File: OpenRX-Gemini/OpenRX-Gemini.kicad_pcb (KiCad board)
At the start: 6 copper layers, 17 x 15.7 mm, 86 parts, among them J1 Conn_Coaxial_Small, J2 Conn_Coaxial_Small, T1 0900PC16J0042001E, T2 0900PC16J0042001E, U1 ESP32-C3, U2 TLV75533PDQNR, U3 LR1121IMLTRT, U4 RFX2401C, U5 SKY13373-460LF, U6 LR1121IMLTRT, U7 RFX2401C, U8 SKY13373-460LF, U9 TS2306A 240GF MSM 9_C2976675, X1 CJ17-400001010B20

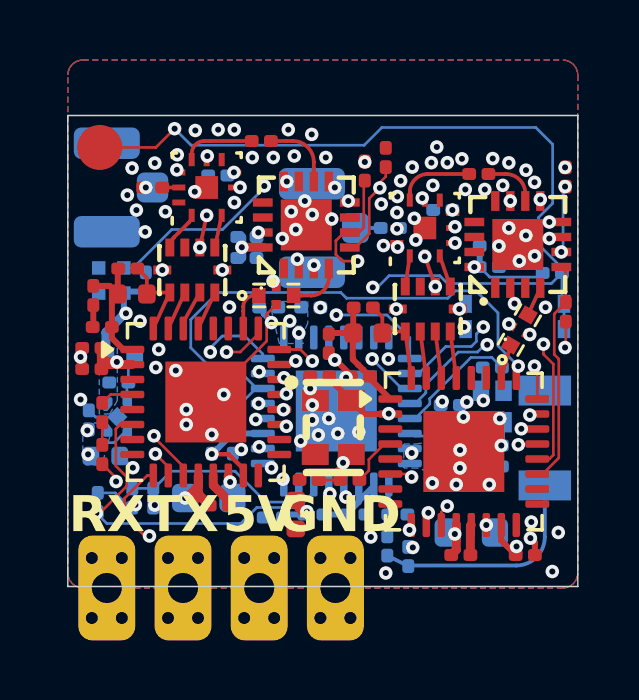
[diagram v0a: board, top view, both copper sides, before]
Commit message: Rev 2 board work: routing optimisations, logo placement, 3D model fixes
Routing reworked on Lite (segments 313 to 256, vias 60 to 89), Lite-UFL
(317 to 269, 61 to 85) and Gemini (682 to 688, 196 to 243). ExpressLRS logo
placed on Mono.

3D model fixes on Gemini and Mono:

- RFX2401C (U4, U7) pointed at QFN-16_L3.0-W3.0-H0.9-P0.50.wrl with an offset
  of (-951.61, 821.31, 0), so the body rendered about a metre off the board and
  the land looked bare in the viewer. Repointed at the RFX2401C model that
  OpenRX-Shared.pretty/QFN-16_L3.0-W3.0-P0.50-BL-EP1.7.kicad_mod specifies,
  offset zeroed, 270 degree rotation kept.
- SKY13373 (U5, U8) carried no model reference at all. Added, matching the
  library footprint.

The boards now agree with the shared library on both, so Update Footprints from
Library preserves this rather than reverting it.

DRC reviewed: zero unconnected items on all four boards. The remaining items
are pre-existing and understood. The shorting_items reports on Lite and
Lite-UFL are all netted-copper against unnetted copper inside the multi-hole
TP footprints, never signal to signal, and are present at the previous commit
too. The copper_edge_clearance reports are the TP1-TP4 castellated pads sitting
on the board edge by design.

Co-Authored-By: Claude Opus 5 (1M context) <noreply@anthropic.com>
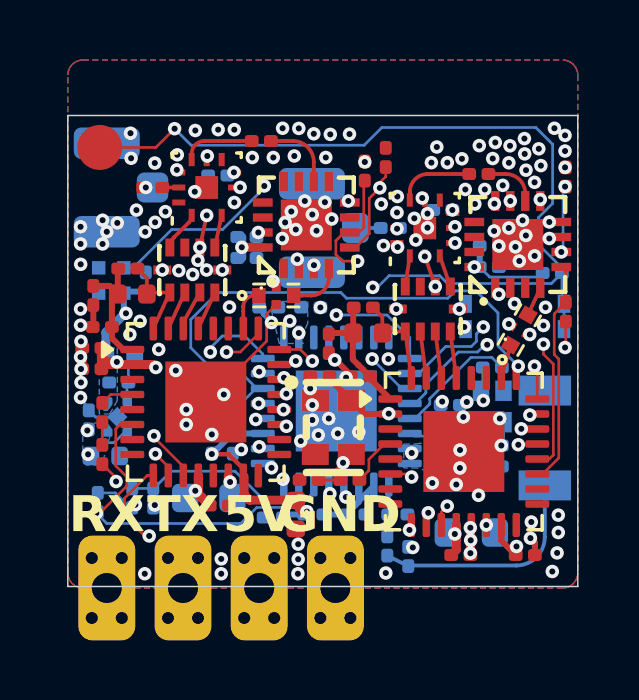
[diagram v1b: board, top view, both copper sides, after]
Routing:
- net GND: track 21.3 -> 19.6 mm, vias 118 -> 165
- net +3V3: track 31.5 -> 32.7 mm
- net Net-(U3-VREG): track 3.03 -> 2.40 mm
